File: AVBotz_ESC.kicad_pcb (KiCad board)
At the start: 4 copper layers, 26 x 32.5 mm, 32 parts, among them J1 Conn_01x04_Pin, J2 Conn_01x03_Pin, Q1 AO3404A, Q2 AO3404A, Q3 AO3404A, Q4 AO3404A, Q5 AO3404A, Q6 AO3404A, U1 ATtiny3227-M, U2 AP63205WU, U3 HIP2100_SOIC, U4 HIP2100_SOIC, U5 HIP2100_SOIC, U6 INA193, U7 INA193

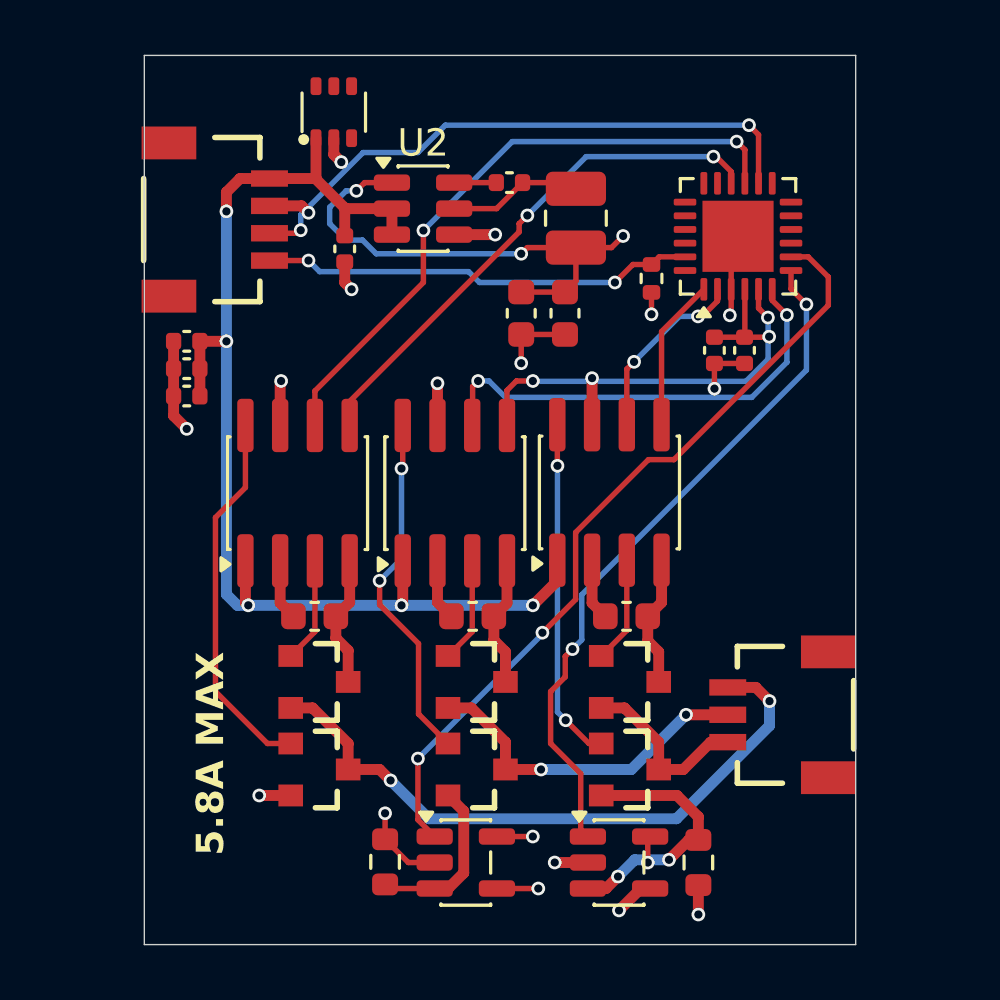
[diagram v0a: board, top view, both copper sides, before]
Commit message: rotate board & RC filters
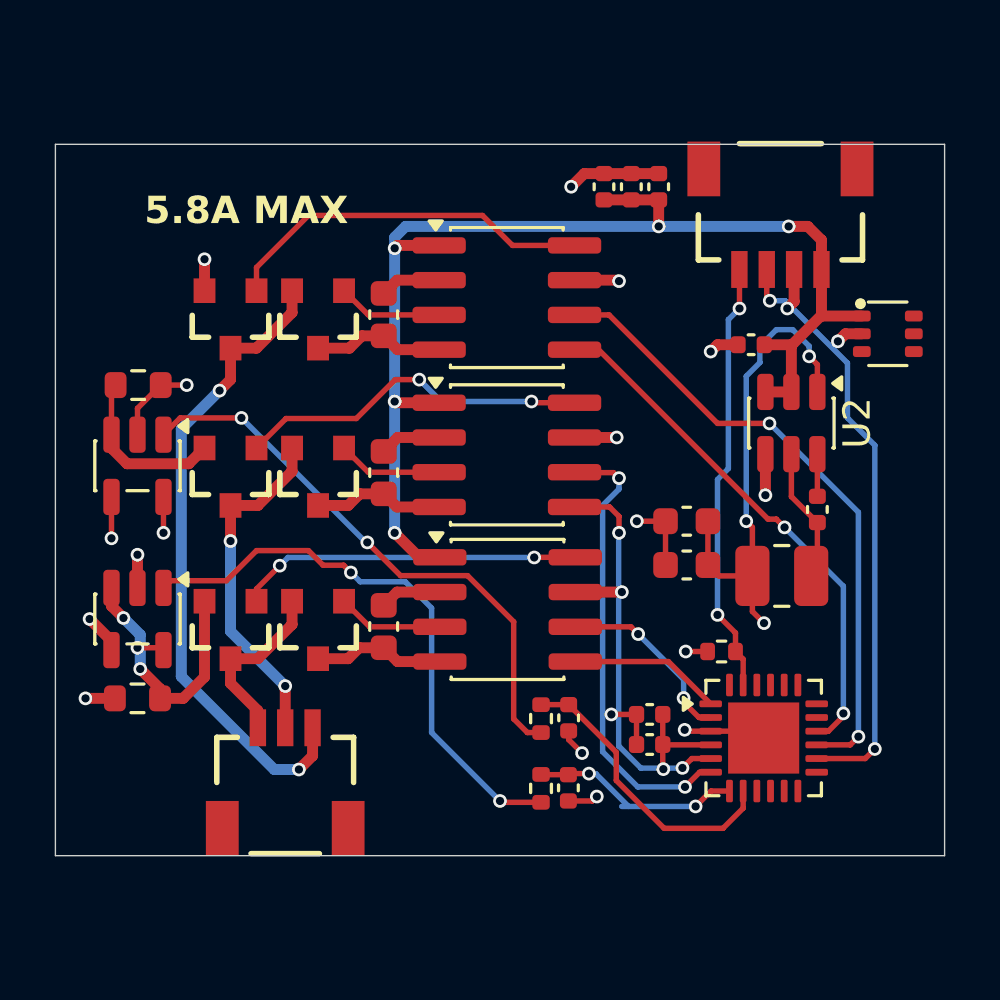
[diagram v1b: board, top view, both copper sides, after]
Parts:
- added C13: 2.2uF, PCM_SparkFun-Capacitor:C_0402_1005Metric, F.Cu at (165.5, 119.3)
- added C14: 2.2uF, PCM_SparkFun-Capacitor:C_0402_1005Metric, F.Cu at (165.5, 116.7)
- added R4: 27, PCM_SparkFun-Resistor:R_0402_1005Metric, F.Cu at (164.5, 119.3)
- added R5: 27, PCM_SparkFun-Resistor:R_0402_1005Metric, F.Cu at (164.5, 116.7)
- moved D2 21.8 mm to (177.2, 102.7), turned to 0 degrees
- moved R2 21.4 mm to (149.8, 116.0), turned to 0 degrees
- moved U6 19.7 mm to (149.8, 113.1), turned to -90 degrees
- moved R3 19.6 mm to (149.8, 104.5), turned to 180 degrees
- moved U7 18.8 mm to (149.8, 107.5), turned to -90 degrees
- moved J1 18.8 mm to (173.2, 100.3), turned to 180 degrees
- moved U1 18.4 mm to (172.6, 117.5), turned to 0 degrees
- moved C11 18.2 mm to (168.8, 97.3), turned to 90 degrees
- moved C12 17.6 mm to (167.8, 97.3), turned to 90 degrees
- moved C7 17.1 mm to (166.8, 97.3), turned to 90 degrees
- moved Q6 16.8 mm to (153.2, 102.1), turned to -90 degrees
- moved C2 16.4 mm to (174.6, 109.1), turned to -90 degrees
- moved J2 16.2 mm to (155.2, 117.1), turned to 0 degrees
- moved U2 15.6 mm to (173.7, 105.9), turned to -90 degrees
- moved Q2 15.4 mm to (153.2, 113.5), turned to -90 degrees
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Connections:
- U6 pad 1: /CSNS1_IN -> Net-(R4-Pad1)
- U7 pad 1: /CSNS2_IN -> Net-(R5-Pad1)
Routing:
- net Net-(R4-Pad1): track 0.00 -> 20.9 mm, vias 0 -> 2
- net Net-(R5-Pad1): track 0.00 -> 20.9 mm, vias 0 -> 2
- net /CSNS2_IN: track 29.1 -> 10.8 mm, vias 2 -> 0
- net /CSNS1_IN: track 25.4 -> 7.87 mm
- net GND: track 101.8 -> 108.0 mm, vias 17 -> 19
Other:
- board size 26 x 32.5 mm -> 32.5 x 26 mm

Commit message: length matching
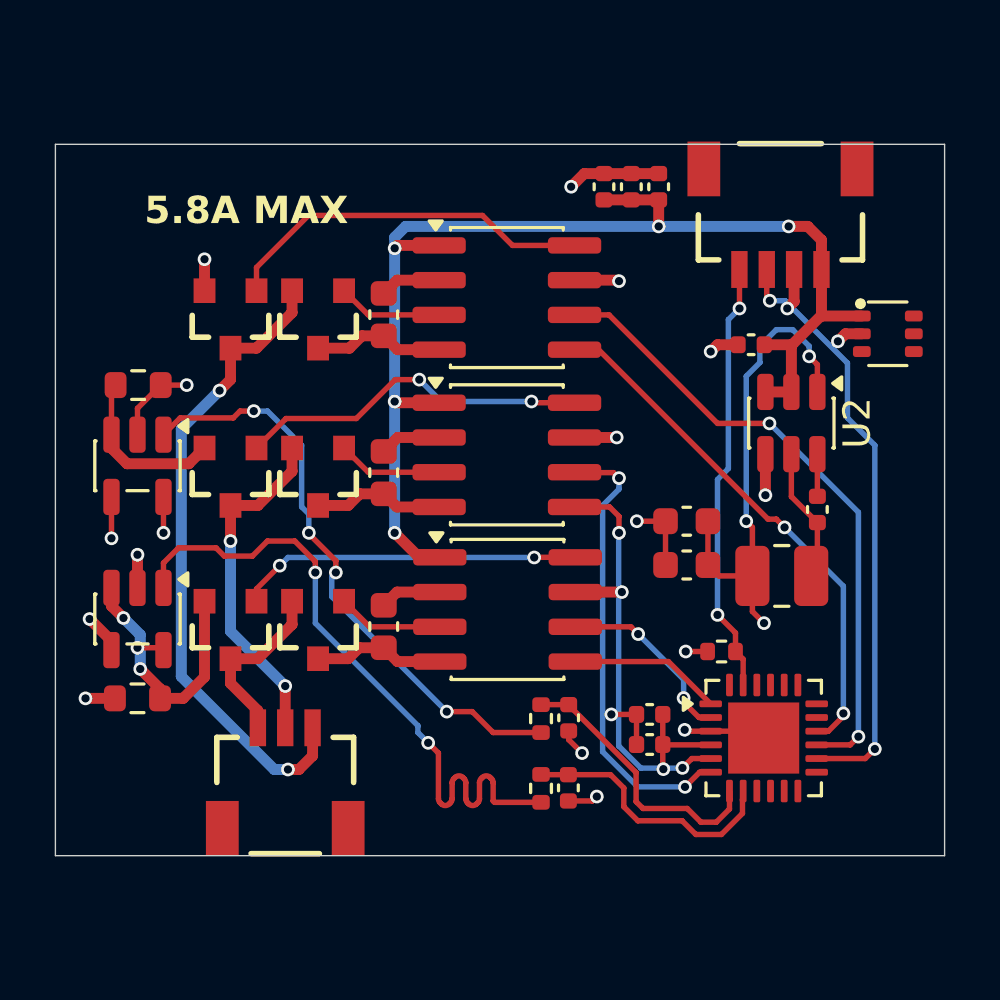
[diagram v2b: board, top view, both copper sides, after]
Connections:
- net Net-(R4-Pad1) renamed /CSD_A
- net Net-(R5-Pad1) renamed /CSD_B
- C13 pad 1: /CSNS1_IN -> /CSNS_A
- C14 pad 1: /CSNS2_IN -> /CSNS_B
- R4 pad 2: /CSNS1_IN -> /CSNS_A
- R5 pad 2: /CSNS2_IN -> /CSNS_B
- U1 pad 7: /CSNS1_IN -> /CSNS_B
- U1 pad 8: /CSNS2_IN -> /CSNS_A
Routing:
- net /CSNS2_IN: track 10.8 -> 0.00 mm
- net /CSNS_B: track 0.00 -> 10.5 mm
- net /CSNS_A: track 0.00 -> 9.86 mm
- net /CSNS1_IN: track 7.87 -> 0.00 mm, vias 2 -> 0
- net /CSD_A: track 20.9 -> 25.2 mm
- net /CSD_B: track 20.9 -> 21.7 mm, vias 2 -> 4

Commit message: code + updates
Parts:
- added H1: MountingHole_Pad, MountingHole:MountingHole_2.2mm_M2_DIN965_Pad, F.Cu at (149.8, 98.8)
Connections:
- U1 pad 11: unconnected-(U1-PB5-Pad11) -> /PWM
- U1 pad 14: /PWM -> unconnected-(U1-PB2-Pad14)
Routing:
- net GND: track 108.0 -> 111.3 mm

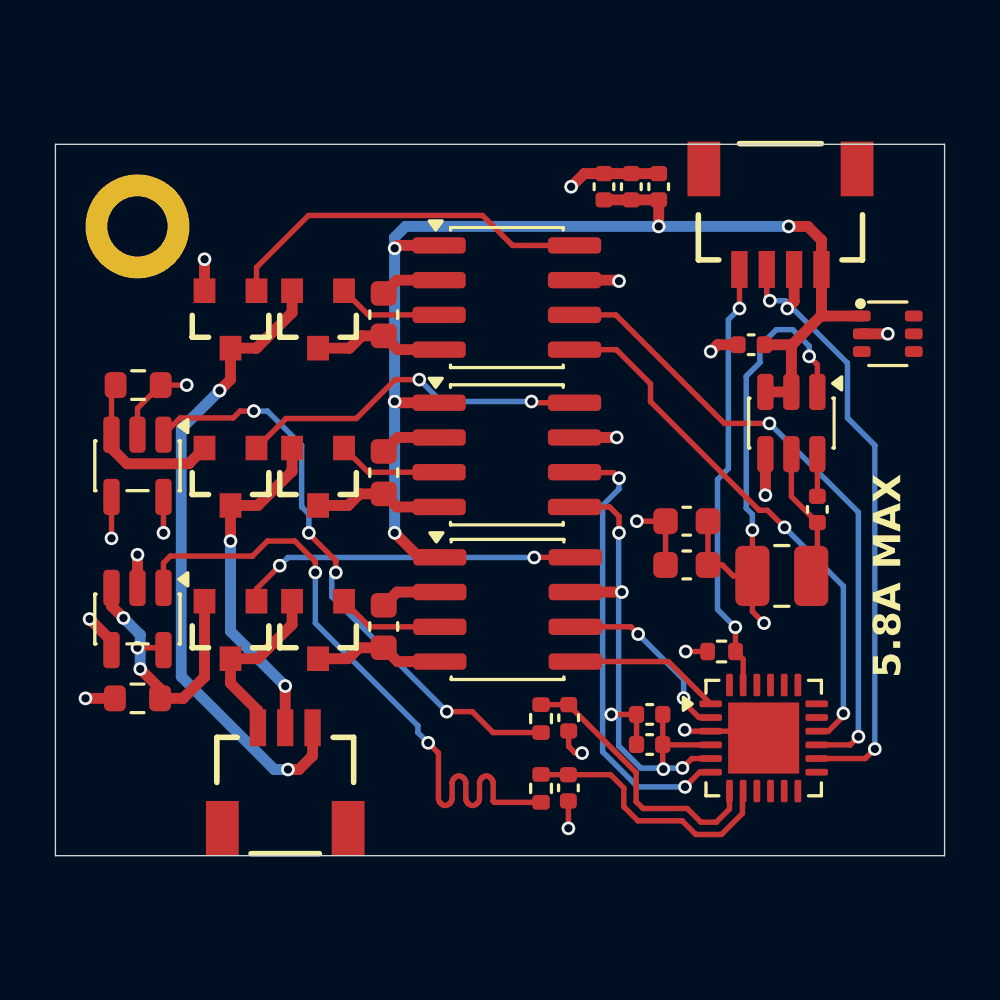
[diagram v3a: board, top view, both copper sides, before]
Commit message: update mosfet wiring
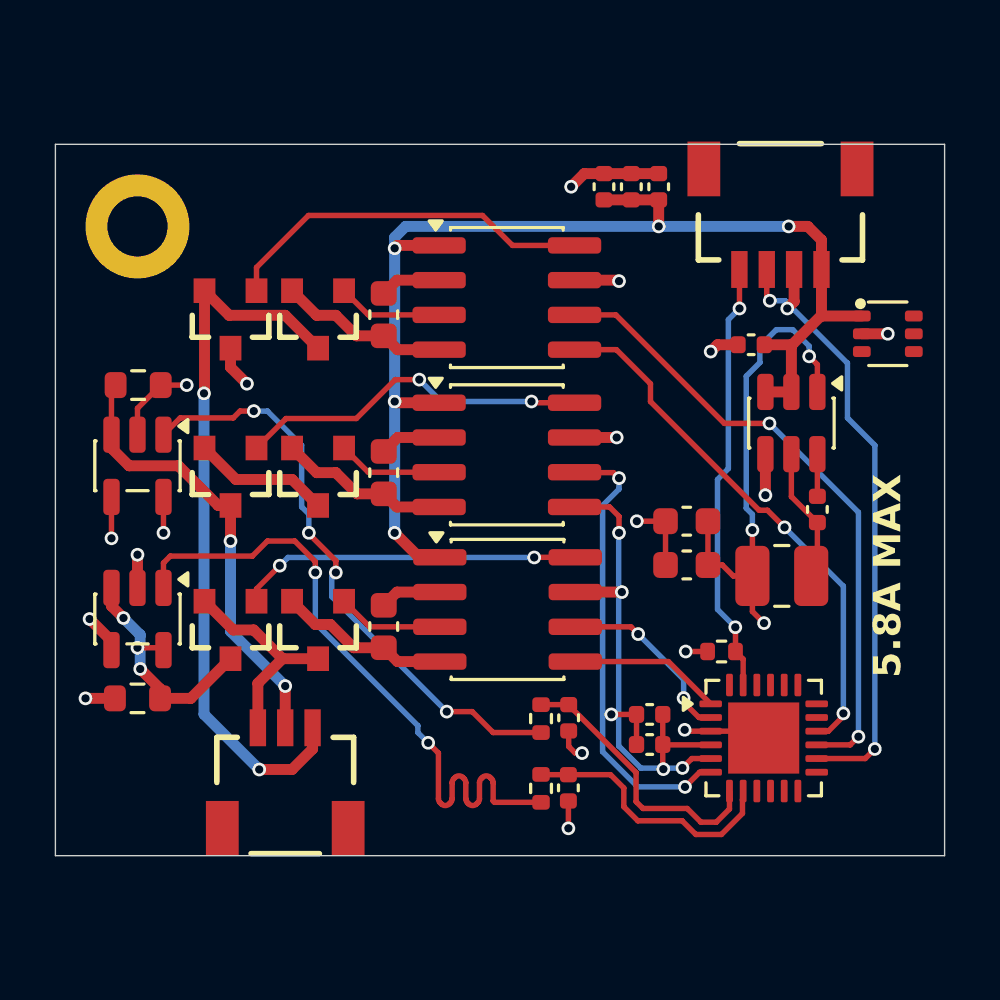
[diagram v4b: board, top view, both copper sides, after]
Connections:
- C10 pad 2: Net-(Q5-D) -> Net-(Q5-S)
- C8 pad 2: Net-(Q1-D) -> Net-(Q1-S)
- C9 pad 2: Net-(Q3-D) -> Net-(Q3-S)
- J2 pad 2: Net-(J2-Pin_2) -> /SHNT2
- Q1 pad 2: Net-(J2-Pin_1) -> Net-(Q1-S)
- Q1 pad 3: Net-(Q1-D) -> Net-(J2-Pin_1)
- Q2 pad 2: /SHNT1 -> Net-(J2-Pin_1)
- Q2 pad 3: Net-(J2-Pin_1) -> /SHNT1
- Q3 pad 2: Net-(J2-Pin_2) -> Net-(Q3-S)
- Q4 pad 2: /SHNT2 -> Net-(Q3-D)
- Q4 pad 3: Net-(J2-Pin_2) -> /SHNT2
- Q5 pad 2: Net-(J2-Pin_3) -> Net-(Q5-S)
- Q5 pad 3: Net-(Q5-D) -> Net-(J2-Pin_3)
- Q6 pad 2: GND -> Net-(J2-Pin_3)
- Q6 pad 3: Net-(J2-Pin_3) -> GND
- U1 pad 11: /PWM -> unconnected-(U1-PB5-Pad11)
- U1 pad 14: unconnected-(U1-PB2-Pad14) -> /PWM
- U3 pad 4: Net-(Q1-D) -> Net-(Q1-S)
- U4 pad 4: Net-(Q3-D) -> Net-(Q3-S)
- U5 pad 4: Net-(Q5-D) -> Net-(Q5-S)
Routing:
- net Net-(J2-Pin_2): track 12.6 -> 0.00 mm, vias 2 -> 0
- net /SHNT2: track 6.24 -> 16.5 mm, vias 0 -> 2
- net Net-(Q1-S): track 0.00 -> 6.31 mm
- net Net-(Q5-S): track 0.00 -> 6.27 mm
- net Net-(Q3-S): track 0.00 -> 6.27 mm
- net Net-(Q1-D): track 4.82 -> 0.00 mm
- net Net-(Q5-D): track 4.82 -> 0.00 mm
- net Net-(J2-Pin_3): track 23.8 -> 26.4 mm
- net /SHNT1: track 9.49 -> 7.95 mm
- net Net-(J2-Pin_1): track 6.56 -> 7.92 mm
